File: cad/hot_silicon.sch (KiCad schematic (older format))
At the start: 37 parts, among them Q303 DTC123Y

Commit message: Placed components. Added possibility of having switches on connector board or circuit board.
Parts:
- added C308: 10n, Capacitors_SMD:C_0603, symbol C
- added C309: 10u, Capacitors_SMD:CP_Elec_5x5.3, symbol CP
- added J304: SW_FAT_B, Pin_Headers:Pin_Header_Straight_1x03_Pitch2.54mm, symbol CONN_01X03
- added R318: 0, Resistors_SMD:R_0603, symbol R
- J301: renamed from J?; footprint (none) -> Pin_Headers:Pin_Header_Straight_2x03_Pitch2.54mm
- J302, J303: renamed from J?; footprint (none) -> Pin_Headers:Pin_Header_Straight_1x06_Pitch2.54mm
- gave numbers to parts that had none: 30
- renumbered D303 to D301, Q303 to Q305, R308 to R317
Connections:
- wire segments 109 -> 119

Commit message: Corrected pots orientation.
Finished layout.
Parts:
- J302, J303: footprint Pin_Headers:Pin_Header_Straight_1x06_Pitch2.54mm -> Pin_Headers:Pin_Header_Straight_1x06_Pitch1.27mm
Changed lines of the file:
@@
 LIBS:contrib
 LIBS:valves
-LIBS:flax_lib
 LIBS:hot_silicon_fuzz-cache
 EELAYER 25 0
@@
 F 3 "" H 4700 3750 50  0001 C CNN
 	1    4700 3750
-	1    0    0    -1
-$EndComp
-$Comp
-L GNDD #PWR019
+	1    0    0    1
+$EndComp
+$Comp
+L GNDD #PWR018
 U 1 1 599CB01A
 P 10400 2500
-F 0 "#PWR019" H 10400 2250 50  0001 C CNN
+F 0 "#PWR018" H 10400 2250 50  0001 C CNN
 F 1 "GNDD" H 10400 2350 50  0000 C CNN
 F 2 "" H 10400 2500 50  0001 C CNN
@@
 $EndComp
 $Comp
-L GNDD #PWR020
+L GNDD #PWR019
 U 1 1 599D14E9
 P 10700 6150
-F 0 "#PWR020" H 10700 5900 50  0001 C CNN
+F 0 "#PWR019" H 10700 5900 50  0001 C CNN
 F 1 "GNDD" H 10700 6000 50  0000 C CNN
 F 2 "" H 10700 6150 50  0001 C CNN
@@
 LED_CMD_B
 $Comp
-L VAA #PWR021
+L VAA #PWR020
 U 1 1 599D4E93
 P 10400 1800
-F 0 "#PWR021" H 10400 1650 50  0001 C CNN
+F 0 "#PWR020" H 10400 1650 50  0001 C CNN
 F 1 "VAA" H 10400 1950 50  0000 C CNN
 F 2 "" H 10400 1800 50  0001 C CNN
@@
 $EndComp
 $Comp
-L VAA #PWR022
+L VAA #PWR021
 U 1 1 599D4F42
 P 10700 4750
-F 0 "#PWR022" H 10700 4600 50  0001 C CNN
+F 0 "#PWR021" H 10700 4600 50  0001 C CNN
 F 1 "VAA" H 10700 4900 50  0000 C CNN
 F 2 "" H 10700 4750 50  0001 C CNN
@@
 $EndComp
 $Comp
-L GNDD #PWR023
+L GNDD #PWR022
 U 1 1 59A4310F
 P 2900 4100
-F 0 "#PWR023" H 2900 3850 50  0001 C CNN
+F 0 "#PWR022" H 2900 3850 50  0001 C CNN
 F 1 "GNDD" H 2900 3950 50  0000 C CNN
 F 2 "" H 2900 4100 50  0001 C CNN
@@
 $EndComp
 $Comp
-L GNDD #PWR024
+L GNDD #PWR023
 U 1 1 59A43380
 P 3300 4100
-F 0 "#PWR024" H 3300 3850 50  0001 C CNN
+F 0 "#PWR023" H 3300 3850 50  0001 C CNN
 F 1 "GNDD" H 3300 3950 50  0000 C CNN
 F 2 "" H 3300 4100 50  0001 C CNN
@@
 $EndComp
 $Comp
-L GNDD #PWR025
+L GNDD #PWR024
 U 1 1 59A445F7
 P 2500 3100
-F 0 "#PWR025" H 2500 2850 50  0001 C CNN
+F 0 "#PWR024" H 2500 2850 50  0001 C CNN
 F 1 "GNDD" H 2500 2950 50  0000 C CNN
 F 2 "" H 2500 3100 50  0001 C CNN
@@
 	2500 3000 2500 3100
 $Comp
-L VAA #PWR026
+L VAA #PWR025
 U 1 1 59A448FC
 P 2500 2500
-F 0 "#PWR026" H 2500 2350 50  0001 C CNN
+F 0 "#PWR025" H 2500 2350 50  0001 C CNN
 F 1 "VAA" H 2500 2650 50  0000 C CNN
 F 2 "" H 2500 2500 50  0001 C CNN
@@
 $EndComp
 $Comp
-L GNDD #PWR027
+L GNDD #PWR026
 U 1 1 59A456AF
 P 4200 4100
-F 0 "#PWR027" H 4200 3850 50  0001 C CNN
+F 0 "#PWR026" H 4200 3850 50  0001 C CNN
 F 1 "GNDD" H 4200 3950 50  0000 C CNN
 F 2 "" H 4200 4100 50  0001 C CNN
@@
 F 3 "" H 4700 4350 50  0001 C CNN
 	1    4700 4350
-	1    0    0    -1
+	1    0    0    1
 $EndComp
 Wire Wire Line
@@
 	4700 3900 4700 4200
 $Comp
-L GNDD #PWR028
+L GNDD #PWR027
 U 1 1 59A46198
 P 4700 4700
-F 0 "#PWR028" H 4700 4450 50  0001 C CNN
+F 0 "#PWR027" H 4700 4450 50  0001 C CNN
 F 1 "GNDD" H 4700 4550 50  0000 C CNN
 F 2 "" H 4700 4700 50  0001 C CNN
@@
 	5200 3750 4850 3750
 $Comp
-L GNDD #PWR029
+L GNDD #PWR028
 U 1 1 59A46456
 P 5200 4400
-F 0 "#PWR029" H 5200 4150 50  0001 C CNN
+F 0 "#PWR028" H 5200 4150 50  0001 C CNN
 F 1 "GNDD" H 5200 4250 50  0000 C CNN
 F 2 "" H 5200 4400 50  0001 C CNN
@@
 Connection ~ 4700 4150
 $Comp
-L VAA #PWR030
+L VAA #PWR029
 U 1 1 59A46648
 P 4200 1900
-F 0 "#PWR030" H 4200 1750 50  0001 C CNN
+F 0 "#PWR029" H 4200 1750 50  0001 C CNN
 F 1 "VAA" H 4200 2050 50  0000 C CNN
 F 2 "" H 4200 1900 50  0001 C CNN
@@
 $EndComp
 $Comp
-L GNDD #PWR031
+L GNDD #PWR030
 U 1 1 59A46D6F
 P 5200 3300
-F 0 "#PWR031" H 5200 3050 50  0001 C CNN
+F 0 "#PWR030" H 5200 3050 50  0001 C CNN
 F 1 "GNDD" H 5200 3150 50  0000 C CNN
 F 2 "" H 5200 3300 50  0001 C CNN
@@
 $EndComp
 $Comp
-L GNDD #PWR032
+L GNDD #PWR031
 U 1 1 59A4860F
 P 6100 1000
-F 0 "#PWR032" H 6100 750 50  0001 C CNN
+F 0 "#PWR031" H 6100 750 50  0001 C CNN
 F 1 "GNDD" H 6100 850 50  0000 C CNN
 F 2 "" H 6100 1000 50  0001 C CNN
@@
 $EndComp
 $Comp
-L GNDD #PWR033
+L GNDD #PWR032
 U 1 1 59A48881
 P 6500 1000
-F 0 "#PWR033" H 6500 750 50  0001 C CNN
+F 0 "#PWR032" H 6500 750 50  0001 C CNN
 F 1 "GNDD" H 6500 850 50  0000 C CNN
 F 2 "" H 6500 1000 50  0001 C CNN
@@
 F 3 "" H 7500 2450 50  0001 C CNN
 	1    7500 2450
-	1    0    0    -1
+	1    0    0    1
 $EndComp
 $Comp
@@
 $EndComp
 $Comp
-L GNDD #PWR034
+L GNDD #PWR033
 U 1 1 59A48C17
 P 7500 3300
-F 0 "#PWR034" H 7500 3050 50  0001 C CNN
+F 0 "#PWR033" H 7500 3050 50  0001 C CNN
 F 1 "GNDD" H 7500 3150 50  0000 C CNN
 F 2 "" H 7500 3300 50  0001 C CNN
@@
 F 3 "" H 7800 2850 50  0001 C CNN
 	1    7800 2850
-	1    0    0    -1
-$EndComp
-$Comp
-L GNDD #PWR035
+	1    0    0    1
+$EndComp
+$Comp
+L GNDD #PWR034
 U 1 1 59A48F09
 P 7800 3300
-F 0 "#PWR035" H 7800 3050 50  0001 C CNN
+F 0 "#PWR034" H 7800 3050 50  0001 C CNN
 F 1 "GNDD" H 7800 3150 50  0000 C CNN
 F 2 "" H 7800 3300 50  0001 C CNN
@@
 F 0 "J302" H 10700 2500 50  0000 C CNN
 F 1 "CONN_SIGNALS_B" V 10800 2150 50  0000 C CNN
-F 2 "Pin_Headers:Pin_Header_Straight_1x06_Pitch2.54mm" H 10700 2150 50  0001 C CNN
+F 2 "Pin_Headers:Pin_Header_Straight_1x06_Pitch1.27mm" H 10700 2150 50  0001 C CNN
 F 3 "" H 10700 2150 50  0001 C CNN
 	1    10700 2150
@@
 F 0 "J303" H 10700 3700 50  0000 C CNN
 F 1 "CONN_SW_EQ_B" V 10800 3350 50  0000 C CNN
-F 2 "Pin_Headers:Pin_Header_Straight_1x06_Pitch2.54mm" H 10700 3350 50  0001 C CNN
+F 2 "Pin_Headers:Pin_Header_Straight_1x06_Pitch1.27mm" H 10700 3350 50  0001 C CNN
 F 3 "" H 10700 3350 50  0001 C CNN
 	1    10700 3350

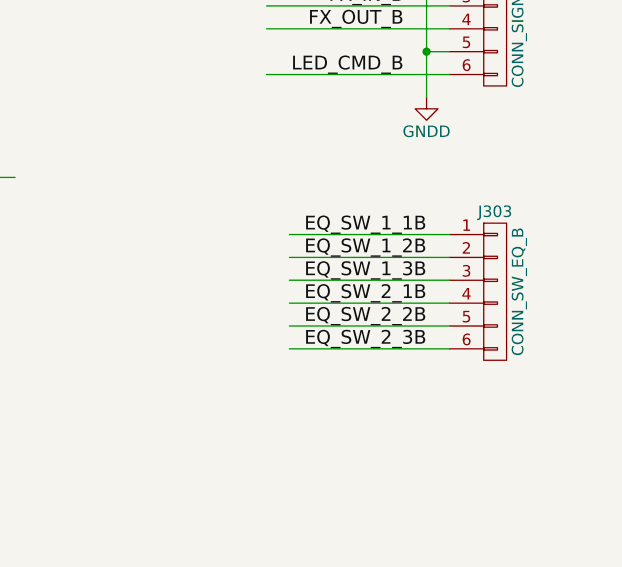
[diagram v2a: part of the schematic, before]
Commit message: Corrected layout
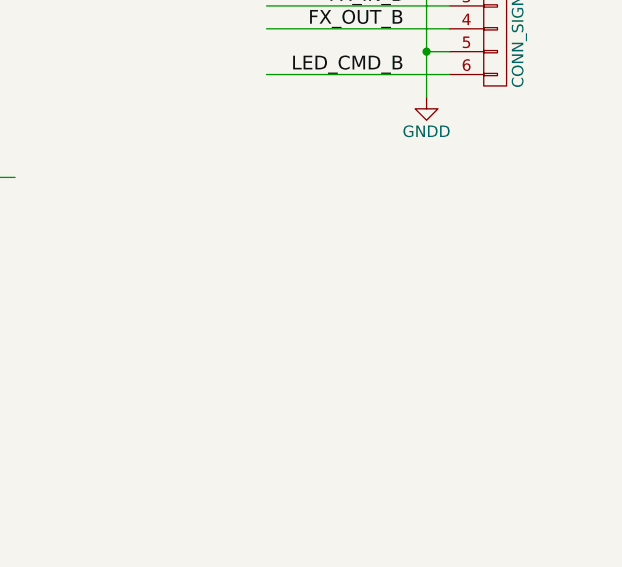
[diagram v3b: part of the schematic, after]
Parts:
- removed J303: CONN_SW_EQ_B, Pin_Headers:Pin_Header_Straight_1x06_Pitch1.27mm, symbol CONN_01X06
- J301: footprint Pin_Headers:Pin_Header_Straight_2x03_Pitch2.54mm -> flax_lib:Multicomp_sub-miniature_DPDT
- J302: footprint Pin_Headers:Pin_Header_Straight_1x06_Pitch1.27mm -> Pin_Headers:Pin_Header_Straight_1x06_Pitch2.54mm
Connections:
- wire segments 119 -> 113
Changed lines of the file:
@@
 LIBS:contrib
 LIBS:valves
+LIBS:flax_lib
 LIBS:hot_silicon_fuzz-cache
 EELAYER 25 0
@@
 $EndComp
 $Comp
-L GNDD #PWR018
+L GNDD #PWR020
 U 1 1 599CB01A
 P 10400 2500
-F 0 "#PWR018" H 10400 2250 50  0001 C CNN
+F 0 "#PWR020" H 10400 2250 50  0001 C CNN
 F 1 "GNDD" H 10400 2350 50  0000 C CNN
 F 2 "" H 10400 2500 50  0001 C CNN
@@
 $EndComp
 $Comp
-L GNDD #PWR019
+L GNDD #PWR021
 U 1 1 599D14E9
 P 10700 6150
-F 0 "#PWR019" H 10700 5900 50  0001 C CNN
+F 0 "#PWR021" H 10700 5900 50  0001 C CNN
 F 1 "GNDD" H 10700 6000 50  0000 C CNN
 F 2 "" H 10700 6150 50  0001 C CNN
@@
 LED_CMD_B
 $Comp
-L VAA #PWR020
+L VAA #PWR022
 U 1 1 599D4E93
 P 10400 1800
-F 0 "#PWR020" H 10400 1650 50  0001 C CNN
+F 0 "#PWR022" H 10400 1650 50  0001 C CNN
 F 1 "VAA" H 10400 1950 50  0000 C CNN
 F 2 "" H 10400 1800 50  0001 C CNN
@@
 $EndComp
 $Comp
-L VAA #PWR021
+L VAA #PWR023
 U 1 1 599D4F42
 P 10700 4750
-F 0 "#PWR021" H 10700 4600 50  0001 C CNN
+F 0 "#PWR023" H 10700 4600 50  0001 C CNN
 F 1 "VAA" H 10700 4900 50  0000 C CNN
 F 2 "" H 10700 4750 50  0001 C CNN
@@
 $EndComp
 $Comp
-L GNDD #PWR022
+L GNDD #PWR024
 U 1 1 59A4310F
 P 2900 4100
-F 0 "#PWR022" H 2900 3850 50  0001 C CNN
+F 0 "#PWR024" H 2900 3850 50  0001 C CNN
 F 1 "GNDD" H 2900 3950 50  0000 C CNN
 F 2 "" H 2900 4100 50  0001 C CNN
@@
 $EndComp
 $Comp
-L GNDD #PWR023
+L GNDD #PWR025
 U 1 1 59A43380
 P 3300 4100
-F 0 "#PWR023" H 3300 3850 50  0001 C CNN
+F 0 "#PWR025" H 3300 3850 50  0001 C CNN
 F 1 "GNDD" H 3300 3950 50  0000 C CNN
 F 2 "" H 3300 4100 50  0001 C CNN
@@
 $EndComp
 $Comp
-L GNDD #PWR024
+L GNDD #PWR026
 U 1 1 59A445F7
 P 2500 3100
-F 0 "#PWR024" H 2500 2850 50  0001 C CNN
+F 0 "#PWR026" H 2500 2850 50  0001 C CNN
 F 1 "GNDD" H 2500 2950 50  0000 C CNN
 F 2 "" H 2500 3100 50  0001 C CNN
@@
 	2500 3000 2500 3100
 $Comp
-L VAA #PWR025
+L VAA #PWR027
 U 1 1 59A448FC
 P 2500 2500
-F 0 "#PWR025" H 2500 2350 50  0001 C CNN
+F 0 "#PWR027" H 2500 2350 50  0001 C CNN
 F 1 "VAA" H 2500 2650 50  0000 C CNN
 F 2 "" H 2500 2500 50  0001 C CNN
@@
 $EndComp
 $Comp
-L GNDD #PWR026
+L GNDD #PWR028
 U 1 1 59A456AF
 P 4200 4100
-F 0 "#PWR026" H 4200 3850 50  0001 C CNN
+F 0 "#PWR028" H 4200 3850 50  0001 C CNN
 F 1 "GNDD" H 4200 3950 50  0000 C CNN
 F 2 "" H 4200 4100 50  0001 C CNN
@@
 	4700 3900 4700 4200
 $Comp
-L GNDD #PWR027
+L GNDD #PWR029
 U 1 1 59A46198
 P 4700 4700
-F 0 "#PWR027" H 4700 4450 50  0001 C CNN
+F 0 "#PWR029" H 4700 4450 50  0001 C CNN
 F 1 "GNDD" H 4700 4550 50  0000 C CNN
 F 2 "" H 4700 4700 50  0001 C CNN
@@
 	5200 3750 4850 3750
 $Comp
-L GNDD #PWR028
+L GNDD #PWR030
 U 1 1 59A46456
 P 5200 4400
-F 0 "#PWR028" H 5200 4150 50  0001 C CNN
+F 0 "#PWR030" H 5200 4150 50  0001 C CNN
 F 1 "GNDD" H 5200 4250 50  0000 C CNN
 F 2 "" H 5200 4400 50  0001 C CNN
@@
 Connection ~ 4700 4150
 $Comp
-L VAA #PWR029
+L VAA #PWR031
 U 1 1 59A46648
 P 4200 1900
-F 0 "#PWR029" H 4200 1750 50  0001 C CNN
+F 0 "#PWR031" H 4200 1750 50  0001 C CNN
 F 1 "VAA" H 4200 2050 50  0000 C CNN
 F 2 "" H 4200 1900 50  0001 C CNN
@@
 $EndComp
 $Comp
-L GNDD #PWR030
+L GNDD #PWR032
 U 1 1 59A46D6F
 P 5200 3300
-F 0 "#PWR030" H 5200 3050 50  0001 C CNN
+F 0 "#PWR032" H 5200 3050 50  0001 C CNN
 F 1 "GNDD" H 5200 3150 50  0000 C CNN
 F 2 "" H 5200 3300 50  0001 C CNN
@@
 $EndComp
 $Comp
-L GNDD #PWR031
+L GNDD #PWR033
 U 1 1 59A4860F
 P 6100 1000
-F 0 "#PWR031" H 6100 750 50  0001 C CNN
+F 0 "#PWR033" H 6100 750 50  0001 C CNN
 F 1 "GNDD" H 6100 850 50  0000 C CNN
 F 2 "" H 6100 1000 50  0001 C CNN
@@
 $EndComp
 $Comp
-L GNDD #PWR032
+L GNDD #PWR034
 U 1 1 59A48881
 P 6500 1000
-F 0 "#PWR032" H 6500 750 50  0001 C CNN
+F 0 "#PWR034" H 6500 750 50  0001 C CNN
 F 1 "GNDD" H 6500 850 50  0000 C CNN
 F 2 "" H 6500 1000 50  0001 C CNN
@@
 $EndComp
 $Comp
-L GNDD #PWR033
+L GNDD #PWR035
 U 1 1 59A48C17
 P 7500 3300
-F 0 "#PWR033" H 7500 3050 50  0001 C CNN
+F 0 "#PWR035" H 7500 3050 50  0001 C CNN
 F 1 "GNDD" H 7500 3150 50  0000 C CNN
 F 2 "" H 7500 3300 50  0001 C CNN
@@
 $EndComp
 $Comp
-L GNDD #PWR034
+L GNDD #PWR036
 U 1 1 59A48F09
 P 7800 3300
-F 0 "#PWR034" H 7800 3050 50  0001 C CNN
+F 0 "#PWR036" H 7800 3050 50  0001 C CNN
 F 1 "GNDD" H 7800 3150 50  0000 C CNN
 F 2 "" H 7800 3300 50  0001 C CNN
@@
 F 0 "J302" H 10700 2500 50  0000 C CNN
 F 1 "CONN_SIGNALS_B" V 10800 2150 50  0000 C CNN
-F 2 "Pin_Headers:Pin_Header_Straight_1x06_Pitch1.27mm" H 10700 2150 50  0001 C CNN
+F 2 "Pin_Headers:Pin_Header_Straight_1x06_Pitch2.54mm" H 10700 2150 50  0001 C CNN
 F 3 "" H 10700 2150 50  0001 C CNN
 	1    10700 2150
@@
 Wire Wire Line
 	10400 2000 10400 2500
-$Comp
-L CONN_01X06 J303
-U 1 1 59A501F7
-P 10700 3350
-F 0 "J303" H 10700 3700 50  0000 C CNN
-F 1 "CONN_SW_EQ_B" V 10800 3350 50  0000 C CNN
-F 2 "Pin_Headers:Pin_Header_Straight_1x06_Pitch1.27mm" H 10700 3350 50  0001 C CNN
-F 3 "" H 10700 3350 50  0001 C CNN
-	1    10700 3350
-	1    0    0    -1
-$EndComp
 Text Label 6400 3650 1    60   ~ 0
 EQ_SW_1_1B
@@
 Text Label 6200 3650 1    60   ~ 0
 EQ_SW_1_3B
-Text Label 10400 3100 2    60   ~ 0
-EQ_SW_1_1B
-Text Label 10400 3200 2    60   ~ 0
-EQ_SW_1_2B
-Text Label 10400 3300 2    60   ~ 0
-EQ_SW_1_3B
-Wire Wire Line
-	10500 3100 9800 3100
-Wire Wire Line
-	9800 3200 10500 3200
-Wire Wire Line
-	10500 3300 9800 3300
 Text Label 6900 3650 1    60   ~ 0
 EQ_SW_2_1B
@@
 Text Label 6700 3650 1    60   ~ 0
 EQ_SW_2_3B
-Text Label 10400 3400 2    60   ~ 0
-EQ_SW_2_1B
-Text Label 10400 3500 2    60   ~ 0
-EQ_SW_2_2B
-Text Label 10400 3600 2    60   ~ 0
-EQ_SW_2_3B
-Wire Wire Line
-	10500 3400 9800 3400
-Wire Wire Line
-	9800 3500 10500 3500
-Wire Wire Line
-	10500 3600 9800 3600
 Wire Wire Line
 	10500 2300 10400 2300
@@
 F 0 "J301" H 6550 4400 50  0000 C CNN
 F 1 "SW_EQ_B" H 6550 4000 50  0000 C CNN
-F 2 "Pin_Headers:Pin_Header_Straight_2x03_Pitch2.54mm" H 6550 3000 50  0001 C CNN
+F 2 "flax_lib:Multicomp_sub-miniature_DPDT" H 6550 3000 50  0001 C CNN
 F 3 "" H 6550 3000 50  0001 C CNN
 	1    6550 4200
